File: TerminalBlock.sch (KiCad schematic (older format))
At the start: 2 parts, among them P4 12-pin Terminal Block, P5 3-pin TB

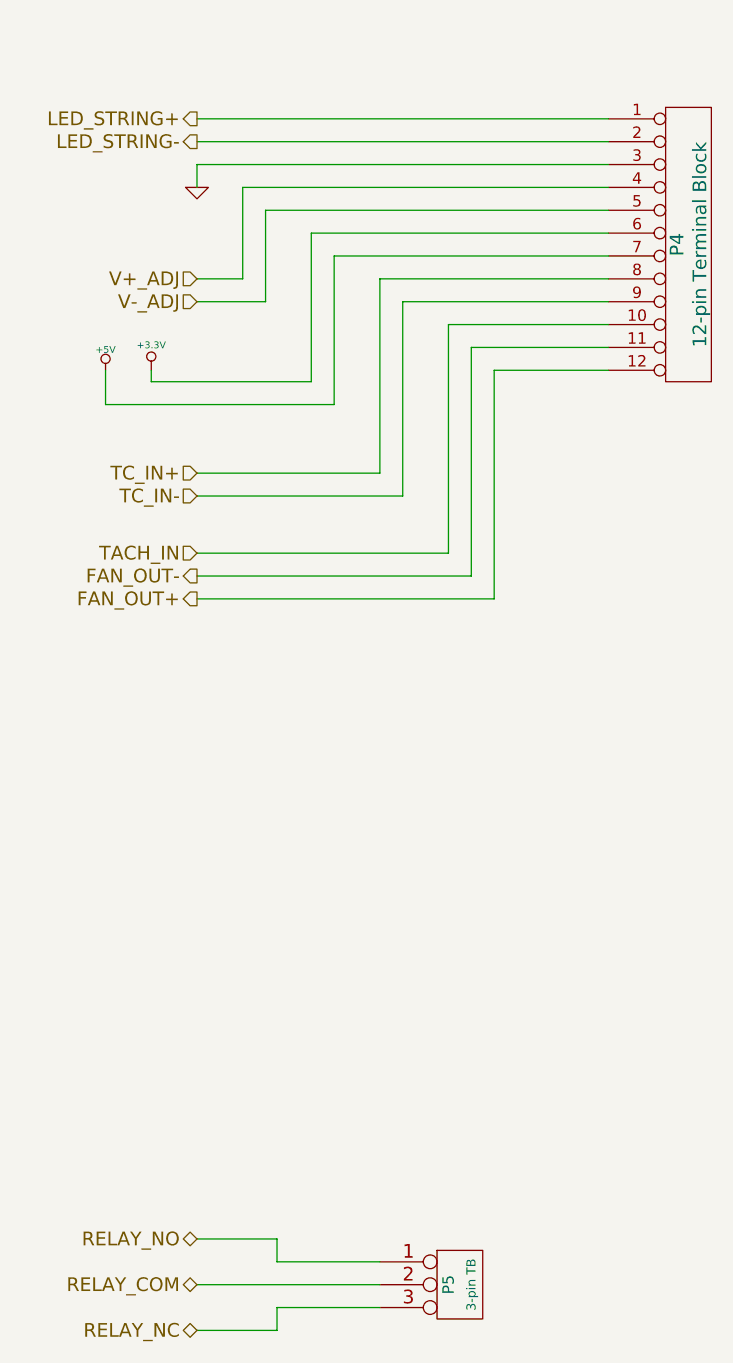
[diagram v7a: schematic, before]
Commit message: Updates from Layout Work Session 4 video
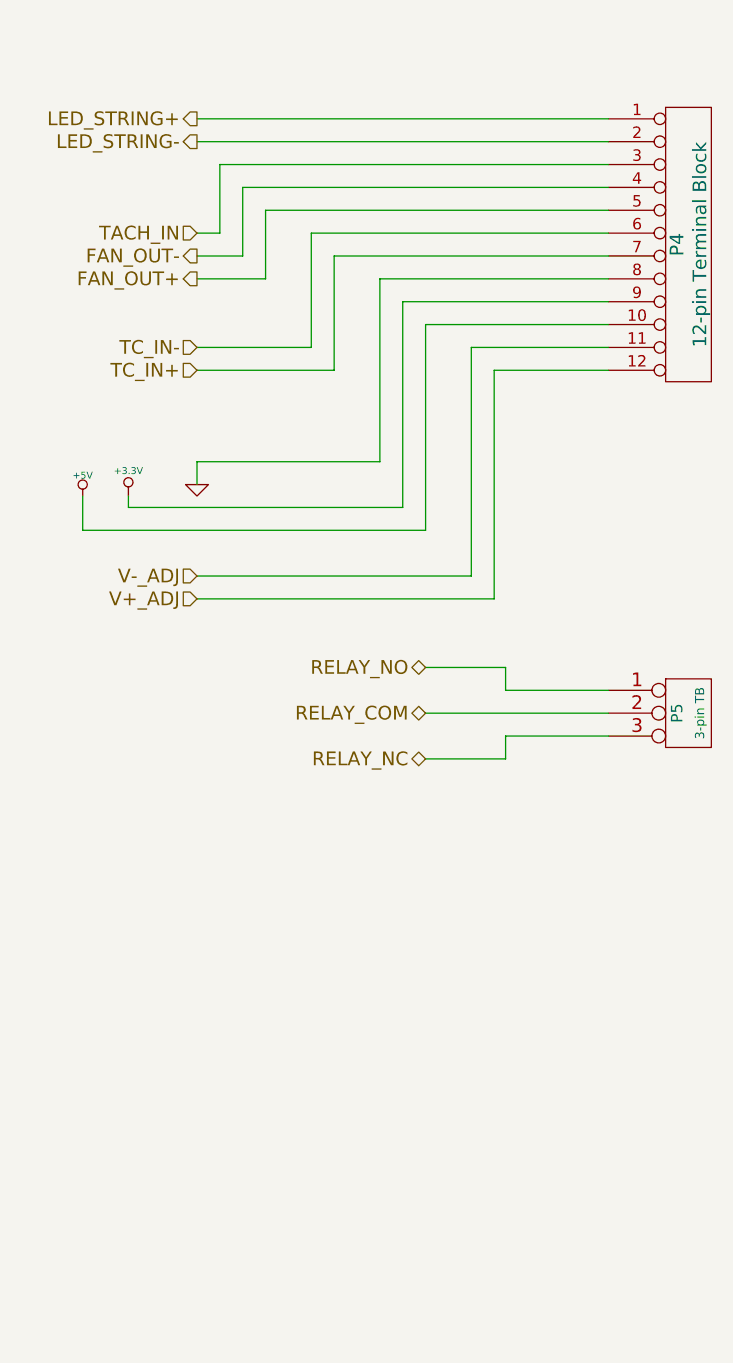
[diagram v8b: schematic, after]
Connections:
- net +3.3V: now also P4.9 (P9); no longer P4.6 (P6)
- net +5V: now also P4.10 (P10); no longer P4.7 (P7)
- net FAN_OUT+: now also P4.5 (P5); no longer P4.12 (P12)
- net FAN_OUT-: now also P4.4 (P4); no longer P4.11 (P11)
- net GND: now also P4.8 (P8); no longer P4.3 (P3)
- net TACH_IN: now also P4.3 (P3); no longer P4.10 (P10)
- net TC_IN+: now also P4.7 (P7); no longer P4.8 (P8)
- net TC_IN-: now also P4.6 (P6); no longer P4.9 (P9)
- net V+_ADJ: now also P4.12 (P12); no longer P4.4 (P4)
- net V-_ADJ: now also P4.11 (P11); no longer P4.5 (P5)
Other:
- moved on the sheet: P5
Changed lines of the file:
@@
 Comment4 ""
 $EndDescr
-Text HLabel 2200 2000 0    60   Input ~ 0
+Text HLabel 2200 3400 0    60   Input ~ 0
 V+_ADJ
-Text HLabel 2200 2100 0    60   Input ~ 0
+Text HLabel 2200 3300 0    60   Input ~ 0
 V-_ADJ
-Text HLabel 2200 3400 0    60   Output ~ 0
+Text HLabel 2200 2000 0    60   Output ~ 0
 FAN_OUT+
-Text HLabel 2200 3300 0    60   Output ~ 0
+Text HLabel 2200 1900 0    60   Output ~ 0
 FAN_OUT-
-Text HLabel 2200 3200 0    60   Input ~ 0
+Text HLabel 2200 1800 0    60   Input ~ 0
 TACH_IN
 Text HLabel 2200 1300 0    60   Output ~ 0
@@
 Text HLabel 2200 1400 0    60   Output ~ 0
 LED_STRING-
-Text HLabel 2200 2850 0    60   Input ~ 0
+Text HLabel 2200 2400 0    60   Input ~ 0
 TC_IN+
-Text HLabel 2200 2950 0    60   Input ~ 0
+Text HLabel 2200 2300 0    60   Input ~ 0
 TC_IN-
-Text HLabel 2200 6400 0    60   BiDi ~ 0
+Text HLabel 3200 3900 0    60   BiDi ~ 0
 RELAY_COM
-Text HLabel 2200 6200 0    60   BiDi ~ 0
+Text HLabel 3200 3700 0    60   BiDi ~ 0
 RELAY_NO
-Text HLabel 2200 6600 0    60   BiDi ~ 0
+Text HLabel 3200 4100 0    60   BiDi ~ 0
 RELAY_NC
 $Comp
 L +3.3V #PWR021
 U 1 1 52FC1D46
-P 2000 2400
-F 0 "#PWR021" H 2000 2360 30  0001 C CNN
-F 1 "+3.3V" H 2000 2510 30  0000 C CNN
-F 2 "" H 2000 2400 60  0000 C CNN
-F 3 "" H 2000 2400 60  0000 C CNN
-	1    2000 2400
+P 1900 2950
+F 0 "#PWR021" H 1900 2910 30  0001 C CNN
+F 1 "+3.3V" H 1900 3060 30  0000 C CNN
+F 2 "" H 1900 2950 60  0000 C CNN
+F 3 "" H 1900 2950 60  0000 C CNN
+	1    1900 2950
 	1    0    0    -1
 $EndComp
@@
 L +5V #PWR022
 U 1 1 52FC1D5A
-P 1800 2400
-F 0 "#PWR022" H 1800 2490 20  0001 C CNN
-F 1 "+5V" H 1800 2490 30  0000 C CNN
-F 2 "" H 1800 2400 60  0000 C CNN
-F 3 "" H 1800 2400 60  0000 C CNN
-	1    1800 2400
+P 1700 2950
+F 0 "#PWR022" H 1700 3040 20  0001 C CNN
+F 1 "+5V" H 1700 3040 30  0000 C CNN
+F 2 "" H 1700 2950 60  0000 C CNN
+F 3 "" H 1700 2950 60  0000 C CNN
+	1    1700 2950
 	1    0    0    -1
 $EndComp
@@
 L GND #PWR023
 U 1 1 52FC1D6E
-P 2200 1600
-F 0 "#PWR023" H 2200 1600 30  0001 C CNN
-F 1 "GND" H 2200 1530 30  0001 C CNN
-F 2 "" H 2200 1600 60  0000 C CNN
-F 3 "" H 2200 1600 60  0000 C CNN
-	1    2200 1600
+P 2200 2900
+F 0 "#PWR023" H 2200 2900 30  0001 C CNN
+F 1 "GND" H 2200 2830 30  0001 C CNN
+F 2 "" H 2200 2900 60  0000 C CNN
+F 3 "" H 2200 2900 60  0000 C CNN
+	1    2200 2900
 	1    0    0    -1
 $EndComp
@@
 L CONN_3 P5
 U 1 1 5308C10D
-P 3350 6400
-F 0 "P5" V 3300 6400 50  0000 C CNN
-F 1 "3-pin TB" V 3400 6400 40  0000 C CNN
-F 2 "" H 3350 6400 60  0000 C CNN
-F 3 "" H 3350 6400 60  0000 C CNN
-F 4 "Phoenix" H 3350 6400 60  0001 C CNN "MFG Name"
-F 5 "1935174" H 3350 6400 60  0001 C CNN "MFG Part Number"
-	1    3350 6400
+P 4350 3900
+F 0 "P5" V 4300 3900 50  0000 C CNN
+F 1 "3-pin TB" V 4400 3900 40  0000 C CNN
+F 2 "" H 4350 3900 60  0000 C CNN
+F 3 "" H 4350 3900 60  0000 C CNN
+F 4 "Phoenix" H 4350 3900 60  0001 C CNN "MFG Name"
+F 5 "1935174" H 4350 3900 60  0001 C CNN "MFG Part Number"
+	1    4350 3900
 	1    0    0    -1
 $EndComp
@@
 	3100 2100 4000 2100
 Wire Wire Line
-	3100 2950 3100 2100
+	3100 3000 3100 2100
 Wire Wire Line
-	2200 2950 3100 2950
+	1900 3000 3100 3000
 Wire Wire Line
 	3000 2000 4000 2000
 Wire Wire Line
-	3000 2850 3000 2000
+	3000 2800 3000 2000
 Wire Wire Line
-	2200 2850 3000 2850
+	2200 2800 3000 2800
 Wire Wire Line
 	2800 1900 4000 1900
 Wire Wire Line
-	2800 2550 2800 1900
+	2800 2400 2800 1900
 Wire Wire Line
-	2200 2100 2500 2100
+	2200 2000 2500 2000
 Wire Wire Line
 	2700 1800 4000 1800
 Wire Wire Line
-	2700 2450 2700 1800
-Wire Wire Line
-	2200 2000 2400 2000
+	2200 1900 2400 1900
 Wire Wire Line
 	2500 1700 4000 1700
 Wire Wire Line
-	2500 2100 2500 1700
+	2500 2000 2500 1700
 Wire Wire Line
-	1800 2550 2800 2550
+	1700 3100 3200 3100
 Wire Wire Line
 	2400 1600 4000 1600
 Wire Wire Line
-	2400 2000 2400 1600
+	2400 1900 2400 1600
 Wire Wire Line
-	2000 2450 2700 2450
+	2300 1500 4000 1500
 Wire Wire Line
-	2200 1500 4000 1500
-Wire Wire Line
-	2200 1600 2200 1500
+	2300 1500 2300 1800
 Wire Wire Line
 	2200 1400 4000 1400
@@
 	2200 1300 4000 1300
 Wire Wire Line
-	2000 2400 2000 2450
+	1900 2950 1900 3000
 Wire Wire Line
-	2200 3200 3300 3200
+	3200 3100 3200 2200
 Wire Wire Line
-	3300 3200 3300 2200
-Wire Wire Line
-	3300 2200 4000 2200
+	3200 2200 4000 2200
 Wire Wire Line
 	2200 3300 3400 3300
@@
 	3500 2400 4000 2400
 Wire Wire Line
-	3000 6300 2550 6300
+	4000 3800 3550 3800
 Wire Wire Line
-	2550 6300 2550 6200
+	3550 3800 3550 3700
 Wire Wire Line
-	2550 6200 2200 6200
+	3550 3700 3200 3700
 Wire Wire Line
-	2200 6400 3000 6400
+	3200 3900 4000 3900
 Wire Wire Line
-	2200 6600 2550 6600
+	3200 4100 3550 4100
 Wire Wire Line
-	2550 6600 2550 6500
+	3550 4100 3550 4000
 Wire Wire Line
-	2550 6500 3000 6500
+	3550 4000 4000 4000
 Wire Wire Line
-	1800 2400 1800 2550
+	1700 2950 1700 3100
+Wire Wire Line
+	2200 2400 2800 2400
+Wire Wire Line
+	2700 2300 2700 1800
+Wire Wire Line
+	2200 2300 2700 2300
+Wire Wire Line
+	2300 1800 2200 1800
+Wire Wire Line
+	2200 2800 2200 2900
 $EndSCHEMATC
